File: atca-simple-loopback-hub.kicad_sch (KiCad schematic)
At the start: 9 parts, among them J10 Conn_Coaxial, J11 Conn_Coaxial, J12 Conn_Coaxial, J13 Conn_Coaxial, J4 Conn_Coaxial, J5 Conn_Coaxial, J8 Conn_Coaxial, J9 Conn_Coaxial

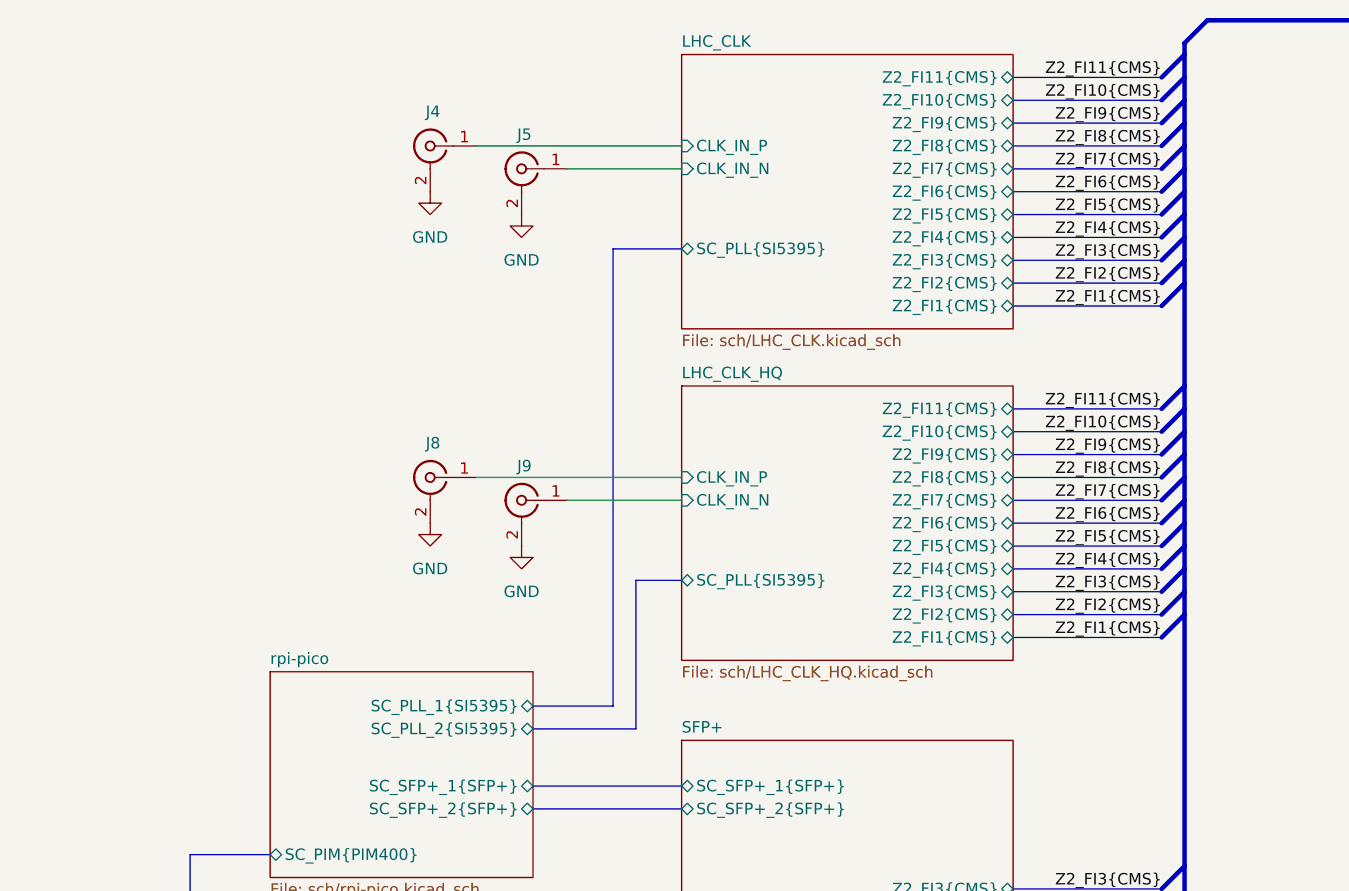
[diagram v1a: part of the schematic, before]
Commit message: added loop between plls and monitoring sma at the second stage pll
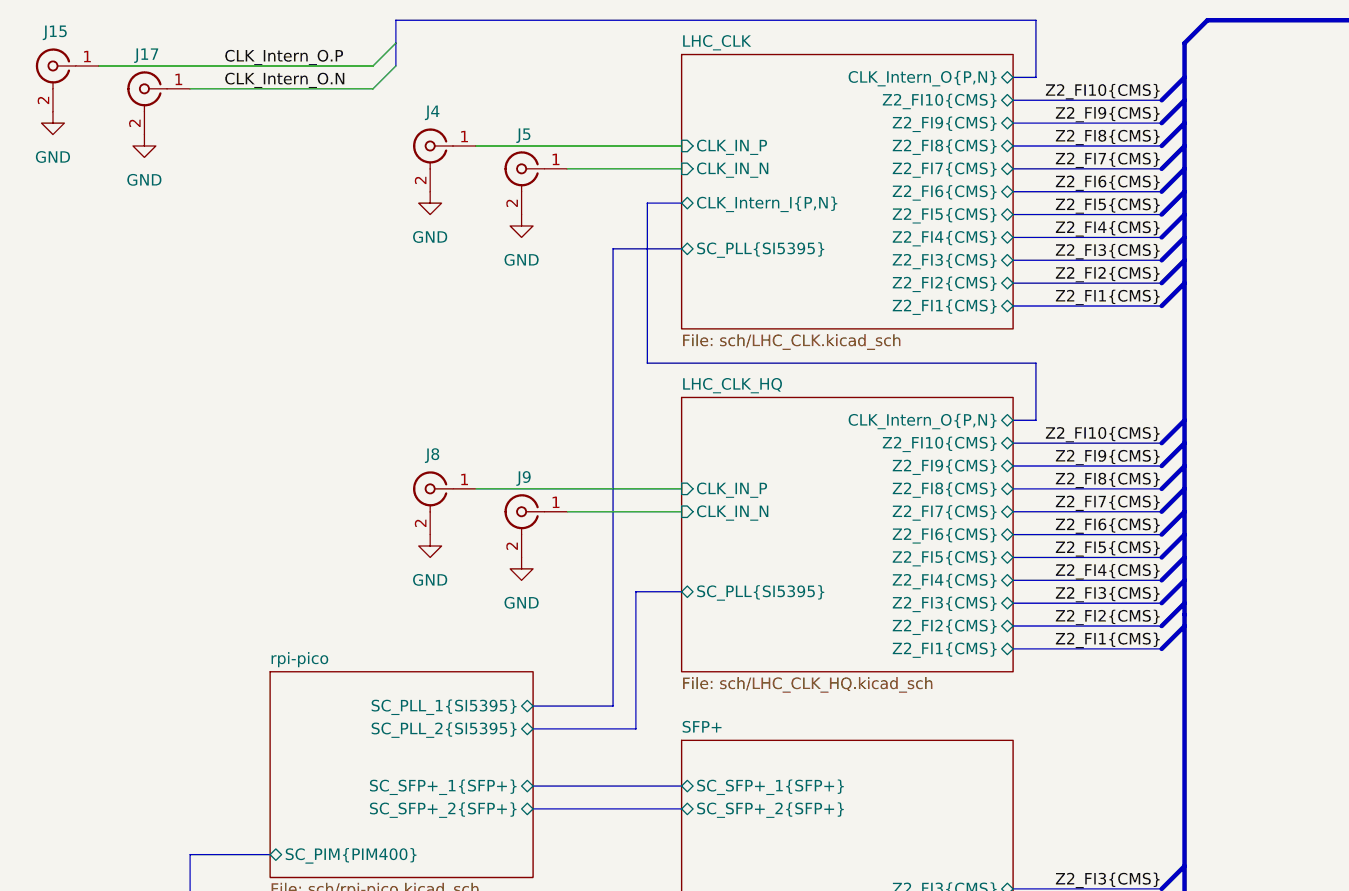
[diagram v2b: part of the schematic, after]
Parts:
- added J15, J17: Conn_Coaxial, Connector_Coaxial:MMCX_Molex_73415-1471_Vertical, symbol Connector:Conn_Coaxial
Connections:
- net GND: now also J15.2 (Ext), J17.2 (Ext)
- new net CLK_Intern_O.N: J17.1 (In)
- new net CLK_Intern_O.P: J15.1 (In)
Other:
- sheet LHC_CLK ports: added CLK_Intern_I{P,N}, CLK_Intern_O{P,N}; removed Z2_FI11{CMS}
- sheet LHC_CLK_HQ ports: added CLK_Intern_O{P,N}; removed Z2_FI11{CMS}
- moved on the sheet: J8, J9

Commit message: all signals routed
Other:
- sheet mech ports: added FP_HANDLE; removed none
- sheet rpi-pico ports: added FP_HANDLE; removed none
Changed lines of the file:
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@@
 		)
 	)
+	(wire
+		(pts
+			(xy 35.56 95.25) (xy 22.86 95.25)
+		)
+		(stroke
+			(width 0)
+			(type default)
+			(color 0 194 194 1)
+		)
+	)
 	(bus
 		(pts
@@
 	(bus
 		(pts
-			(xy 163.83 172.72) (xy 163.83 135.89)
+			(xy 163.83 170.18) (xy 163.83 135.89)
 		)
 		(stroke
@@
 	(bus
 		(pts
-			(xy 33.02 106.68) (xy 33.02 172.72)
+			(xy 26.67 106.68) (xy 26.67 170.18)
 		)
 		(stroke
@@
 		)
 	)
+	(wire
+		(pts
+			(xy 22.86 173.99) (xy 40.64 173.99)
+		)
+		(stroke
+			(width 0)
+			(type default)
+			(color 0 194 194 1)
+		)
+	)
 	(bus
 		(pts
@@
 	(bus
 		(pts
-			(xy 33.02 172.72) (xy 163.83 172.72)
+			(xy 26.67 170.18) (xy 163.83 170.18)
 		)
 		(stroke
@@
 		)
 	)
+	(wire
+		(pts
+			(xy 40.64 180.34) (xy 38.1 180.34)
+		)
+		(stroke
+			(width 0)
+			(type default)
+			(color 0 194 194 1)
+		)
+	)
 	(bus
 		(pts
@@
 		)
 	)
+	(wire
+		(pts
+			(xy 40.64 173.99) (xy 40.64 180.34)
+		)
+		(stroke
+			(width 0)
+			(type default)
+			(color 0 194 194 1)
+		)
+	)
 	(bus
 		(pts
@@
 		)
 	)
+	(wire
+		(pts
+			(xy 22.86 95.25) (xy 22.86 173.99)
+		)
+		(stroke
+			(width 0)
+			(type default)
+			(color 0 194 194 1)
+		)
+	)
 	(bus
 		(pts
-			(xy 41.91 106.68) (xy 33.02 106.68)
+			(xy 35.56 106.68) (xy 26.67 106.68)
 		)
 		(stroke
@@
 	)
 	(sheet
-		(at 41.91 86.36)
-		(size 29.21 22.86)
+		(at 35.56 86.36)
+		(size 35.56 22.86)
 		(fields_autoplaced yes)
 		(stroke
@@
 		)
 		(property "Sheetname" "rpi-pico"
-			(at 41.91 85.6484 0)
+			(at 35.56 85.6484 0)
 			(effects
 				(font
@@
 		)
 		(property "Sheetfile" "sch/rpi-pico.kicad_sch"
-			(at 41.91 109.8046 0)
+			(at 35.56 109.8046 0)
 			(effects
 				(font
@@
 		)
 		(pin "SC_PIM{PIM400}" bidirectional
-			(at 41.91 106.68 180)
+			(at 35.56 106.68 180)
 			(effects
 				(font
@@
 			)
 		)
+		(pin "FP_HANDLE" output
+			(at 35.56 95.25 180)
+			(effects
+				(font
+					(size 1.27 1.27)
+				)
+				(justify left)
+			)
+		)
 		(instances
 			(project "atca-simple-loopback-hub"
@@
 			)
 		)
+		(pin "FP_HANDLE" output
+			(at 38.1 180.34 0)
+			(effects
+				(font
+					(size 1.27 1.27)
+				)
+				(justify right)
+			)
+		)

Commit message: v1.0 as fabricated
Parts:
- G1: footprint project:KIT_LOGO -> project:KIT_LOGO_Mask
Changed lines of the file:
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@@
 	(title_block
 		(title "ATCA Simple Loopback HUB")
-		(date "2024-09-04")
+		(date "2024-09-18")
 		(rev "1.0")
 		(company "Karlsruhe Institute of Technology (KIT)")
 		(comment 1 "Institute for Data Processing and Electronics (IPE)")
 		(comment 2 "Luis Ardila-Perez")
-		(comment 3 "IPE-380-06-V1")
+		(comment 3 "IPE-380-09-V1")
 		(comment 4 "Licensed under CERN-OHL-P-2.0")
+		(comment 5 "https://github.com/kit-ipe/atca-simple-loopback-hub")
+		(comment 6 "https://gitlab.cern.ch/kit-ipe/hardware/kicad-pcbs/atca-simple-loopback-hub")
 	)
 	(no_connect
@@
 			)
 		)
-		(property "Footprint" "project:KIT_LOGO"
+		(property "Footprint" "project:KIT_LOGO_Mask"
 			(at 267.97 173.99 0)
 			(effects
